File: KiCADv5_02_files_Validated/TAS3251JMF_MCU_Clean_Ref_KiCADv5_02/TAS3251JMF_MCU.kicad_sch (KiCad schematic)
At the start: 0 parts

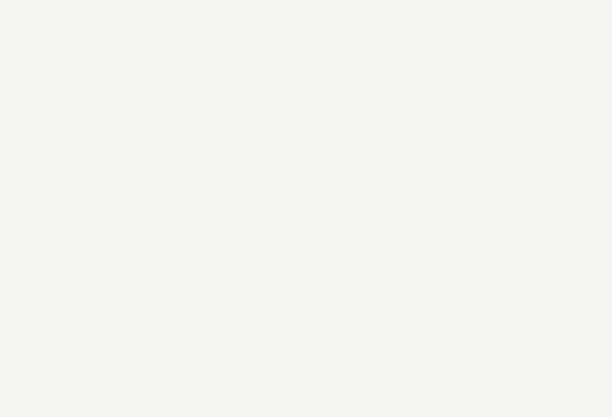
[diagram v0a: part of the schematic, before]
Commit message: Separating SCHs
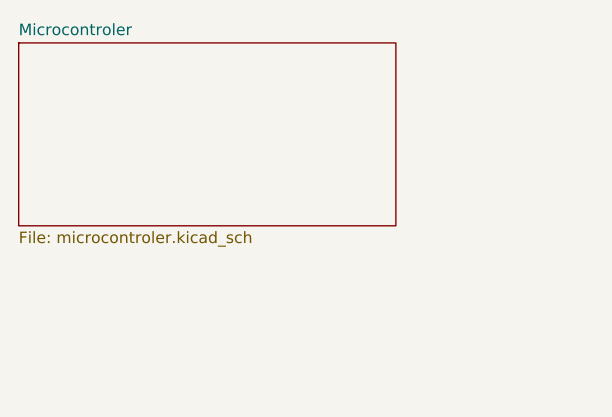
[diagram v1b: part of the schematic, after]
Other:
- added sheet Microcontroler (microcontroler.kicad_sch)
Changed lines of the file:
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@@
+		)
+	)
+	(sheet
+		(at 60.96 64.77)
+		(size 41.91 20.32)
+		(exclude_from_sim no)
+		(in_bom yes)
+		(on_board yes)
+		(dnp no)
+		(fields_autoplaced yes)
+		(stroke
+			(width 0.1524)
+			(type solid)
+		)
+		(fill
+			(color 0 0 0 0.0000)
+		)
+		(property "Sheetname" "Microcontroler"
+			(at 60.96 64.0584 0)
+			(effects
+				(font
+					(size 1.27 1.27)
+				)
+				(justify left bottom)
+			)
+		)
+		(property "Sheetfile" "microcontroler.kicad_sch"
+			(at 60.96 85.6746 0)
+			(effects
+				(font
+					(size 1.27 1.27)
+				)
+				(justify left top)
+			)
+		)
+		(instances
+			(project "TAS3251JMF_MCU"
+				(path "/670752d9-b643-4a78-8b5c-6f0582e4ca27"
+					(page "4")
+				)
+			)
 		)
 	)

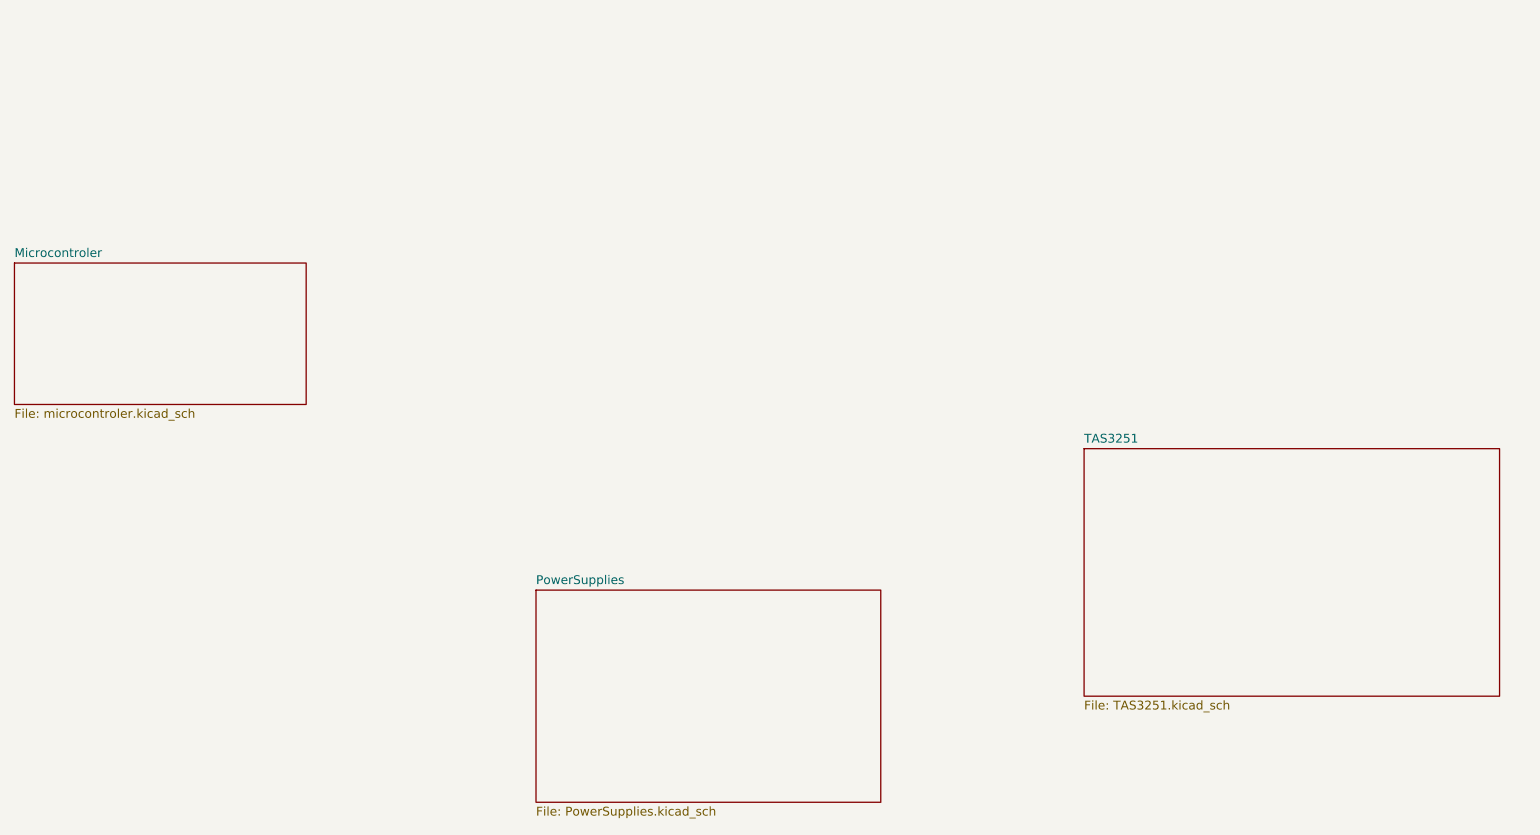
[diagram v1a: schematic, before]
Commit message: Adding new uC module
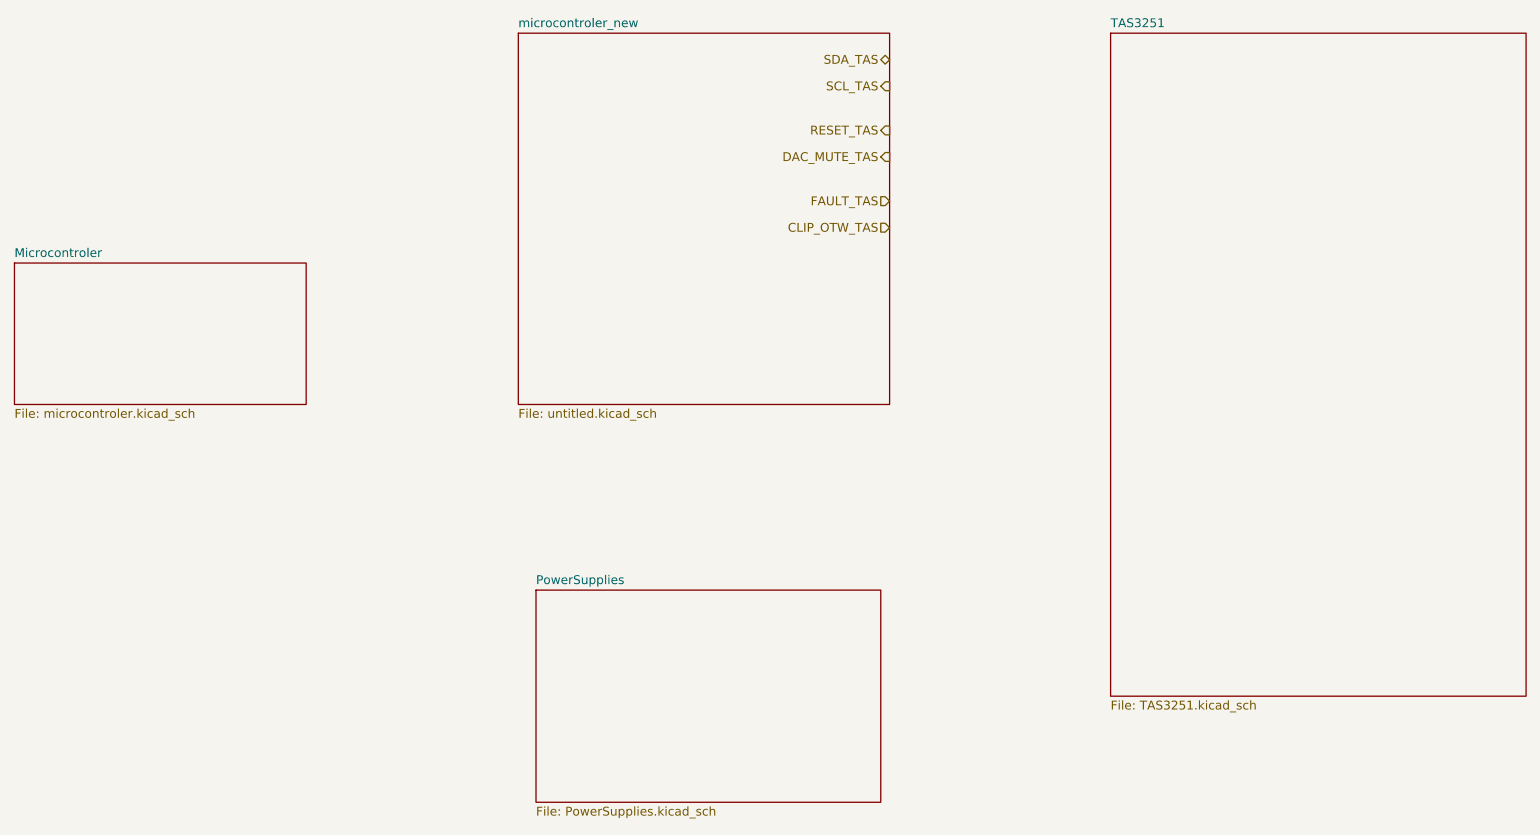
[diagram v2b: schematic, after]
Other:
- added sheet microcontroler_new (untitled.kicad_sch)
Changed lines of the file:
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@@
 		(comment 1 "Licence: CC BY-SA 4.0")
 	)
-	(sheet
-		(at 214.63 91.44)
-		(size 59.69 35.56)
+	(hierarchical_label "CLIP_OTW_TAS"
+		(shape input)
+		(at 186.69 59.69 180)
+		(effects
+			(font
+				(size 1.27 1.27)
+			)
+			(justify right)
+		)
+	)
+	(hierarchical_label "FAULT_TAS"
+		(shape input)
+		(at 186.69 55.88 180)
+		(effects
+			(font
+				(size 1.27 1.27)
+			)
+			(justify right)
+		)
+	)
+	(hierarchical_label "SCL_TAS"
+		(shape output)
+		(at 186.69 39.37 180)
+		(effects
+			(font
+				(size 1.27 1.27)
+			)
+			(justify right)
+		)
+	)
+	(hierarchical_label "RESET_TAS"
+		(shape output)
+		(at 186.69 45.72 180)
+		(effects
+			(font
+				(size 1.27 1.27)
+			)
+			(justify right)
+		)
+	)
+	(hierarchical_label "SDA_TAS"
+		(shape bidirectional)
+		(at 186.69 35.56 180)
+		(effects
+			(font
+				(size 1.27 1.27)
+			)
+			(justify right)
+		)
+	)
+	(hierarchical_label "DAC_MUTE_TAS"
+		(shape output)
+		(at 186.69 49.53 180)
+		(effects
+			(font
+				(size 1.27 1.27)
+			)
+			(justify right)
+		)
+	)
+	(sheet
+		(at 218.44 31.75)
+		(size 59.69 95.25)
 		(exclude_from_sim no)
 		(in_bom yes)
@@
 		)
 		(property "Sheetname" "TAS3251"
-			(at 214.63 90.7284 0)
+			(at 218.44 31.0384 0)
 			(effects
 				(font
@@
 		)
 		(property "Sheetfile" "TAS3251.kicad_sch"
-			(at 214.63 127.5846 0)
+			(at 218.44 127.5846 0)
 			(effects
 				(font
@@
 				)
 			)
+		)
+	)
+	(sheet
+		(at 133.35 31.75)
+		(size 53.34 53.34)
+		(exclude_from_sim no)
+		(in_bom yes)
+		(on_board yes)
+		(dnp no)
+		(fields_autoplaced yes)
+		(stroke
+			(width 0.1524)
+			(type solid)
+		)
+		(fill
+			(color 0 0 0 0.0000)
+		)
+		(property "Sheetname" "microcontroler_new"
+			(at 133.35 31.0384 0)
+			(effects
+				(font
+					(size 1.27 1.27)
+				)
+				(justify left bottom)
+			)
+		)
+		(property "Sheetfile" "untitled.kicad_sch"
+			(at 133.35 85.6746 0)
+			(effects
+				(font
+					(size 1.27 1.27)
+				)
+				(justify left top)
+			)
+		)
+		(instances
+			(project "TAS3251JMF_MCU"
+				(path "/670752d9-b643-4a78-8b5c-6f0582e4ca27"
+					(page "5")
+				)
+			)

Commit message: adding components
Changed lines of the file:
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@@
 		(comment 1 "Licence: CC BY-SA 4.0")
 	)
-	(hierarchical_label "CLIP_OTW_TAS"
+	(hierarchical_label "\\CLIP_OTW"
 		(shape input)
 		(at 186.69 59.69 180)
@@
 		)
 	)
-	(hierarchical_label "FAULT_TAS"
+	(hierarchical_label "\\FAULT"
 		(shape input)
 		(at 186.69 55.88 180)
